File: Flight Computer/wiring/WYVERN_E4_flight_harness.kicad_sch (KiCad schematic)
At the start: 0 parts

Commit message: Commit!
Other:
- note added: "BATTERY SENSE (GP26 / ADC0)"
- note added: "GP26: ADC0 battery divider (100k/62k)"
- note added: "GP26: ADC0 node, ratio 0.3827 (8.4V -> 3.21V)"
- note added: "GP28: ADC2 spare (unwired)"
- note added: "R_BOT: 62k -> GND"
- note added: "R_TOP: 100k -> ADC node"
- note added: "VBAT_TAP: pack + (before UBEC)"
- note added: "warn 6.4V (3.2V/cell) / arm-inhibit 6.0V (3.0V/cell)"
- title: WYVERN-E 4.0 — RPi Pico 2 W flight harness -> WYVERN-E — RPi Pico 2 W flight harness

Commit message: Update - but the PCB no work :(
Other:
- note added: "+V (buck rail)"
- note added: "3V3(?)/GND: full-rate flight log"
- note added: "3V3: logic + sensor rail"
- note added: "A1 addr pin: traces to ~5V (R10/U13 node), not a valid GND/VS+/SDA/SCL strap"
- note added: "AP2112K-3.3 LDO -> 3V3 logic"
- note added: "BME680 (0x76 CONFIRMED, shared bus)"
- note added: "GP0/GP1: shared I2C -> body BNO055, external BNO085 (STEMMA-QT), BME680, INA226, LIS3MDL"
- note added: "GP12: reserved for RBF, NOT wired to any switch on this board rev"
- note added: "GP2: PWM servo1 (pitch, JST U8)"
- note added: "GP34: buzzer (H1 pin10, confirmed GPIO)"
- note added: "GP35: status LED (H1 pin9, confirmed GPIO)"
- note added: "GP36: CAM_EN gate (H1 pin8, confirmed GPIO)"
- note added: "GP37: LAUNCH_IRQ (H1 pin7, confirmed GPIO)"
- note added: "GP3: PWM servo2 (yaw, JST U9)"
- note added: "GP4/GP5: spare JST (U10/U11, function TBD)"
- note added: "GP8/GP9/GP10/GP11: microSD (MISO/CS/SCK/MOSI, all 4 pins confirmed)"
- note added: "IMUs x2, shared bus (different chip families)"
- note added: "INA226 POWER MONITOR (U4, shared I2C bus) -- WIRING PROBLEM, SEE CONFLICTS.md"
- note added: "LIS3MDL (0x1C CONFIRMED, shared bus)"
- note added: "MISO GP8 / CS GP9 / SCK GP10 / MOSI GP11 -- all confirmed (fixed a MOSI/CS swap from an earlier pass)"
- note added: "RP2350B (U1, bare QFN-80, custom PCB1)"
- note added: "S1_SIG: GP2 (JST U8)"
- note added: "S2_SIG: GP3 (JST U9)"
- note added: "SDO->GND, CSB->3V3 (I2C mode) -- pressure/temp/gas, no BMP388 populated"
- note added: "SDO/SA1->GND -- magnetometer, present on PCB1, unused by firmware"
- note added: "STORAGE, microSD (CARD1, TF-01A) -- POSSIBLE DEFECT, SEE CONFLICTS.md"
- note added: "TPS564201 buck -> intermediate rail"
- note added: "V(buck): gated by CAM_EN (GP36)"
- note added: "VBUS/VIN-: trace to the ~5V BUCK OUTPUT rail, not pack voltage"
- note added: "VIN+: traces to GND -- no real shunt in this path, current/power not meaningful"
- note added: "address 0x40 is a bench-scan starting guess, not confirmed"
- note added: "body: BNO055 0x28 CONFIRMED (COM3/ADR -> GND)"
- note added: "external: BNO085 0x4A (SH2 protocol, STEMMA-QT, bulkhead-boundary mount, not on the gimbal)"
- note added: "getBusVoltage() -> battery.h, rail-sag thresholds only (NOT LiPo pack protection)"
- note added: "no WiFi/BLE chip on this board -- wifi_telemetry.h compiled only if WIFI_ENABLED"
- note added: "pin4 (expected VDD) traces to GND in the netlist, not 3V3 -- bench-check before trusting SD logging"
- note added: "servo/expansion connectors (U8-U11) off buck rail"
- note removed: "+5V (UBEC rail)"
- note removed: "3V3 / GND: full-rate flight log"
- note removed: "3V3: sensor rail"
- note removed: "BATTERY SENSE (GP26 / ADC0)"
- note removed: "CYW43: WiFi/BLE bench telemetry"
- note removed: "GP14: PWM servo1 (pitch)"
- note removed: "GP15: PWM servo2 (yaw)"
- note removed: "GP16/GP17: I2C0 -> PCA9548A mux"
- note removed: "GP18/GP19: I2C1 -> gimbal BNO085"
- note removed: "GP2/3/4/5: SPI0 microSD (SCK/MOSI/MISO/CS)"
- note removed: "GP22: RBF sense"
- note removed: "GP26: ADC0 battery divider (100k/62k)"
- note removed: "GP26: ADC0 node, ratio 0.3827 (8.4V -> 3.21V)"
- note removed: "GP28: ADC2 spare (unwired)"
- note removed: "GP6/GP1: spare (RRC3 removed — motor ejection)"
- note removed: "GP7: LAUNCH_IRQ"
- note removed: "GP8: CAM_EN gate"
- note removed: "GP9: LED GP10: buzzer"
- note removed: "IMUs x3 (BNO085, Game Rotation Vector)"
- note removed: "PCA9548A I2C MUX (0x70, on I2C0)"
- note removed: "RPi PICO 2 W (RP2350, FC + real-time TVC)"
- note removed: "R_BOT: 62k -> GND"
- note removed: "R_TOP: 100k -> ADC node"
- note removed: "S1_SIG: GP14"
- note removed: "S2_SIG: GP15"
- note removed: "SCK GP2 / MOSI GP3 / MISO GP4 / CS GP5"
- note removed: "STORAGE — microSD (SPI0 breakout)"
- note removed: "V5: 5V UBEC -> Pico VSYS/cam/servos"
- note removed: "V5: gated by CAM_EN (GP8)"
- note removed: "VBAT_TAP: pack + (before UBEC)"
- note removed: "VSYS: 5V in"
- note removed: "body(FC): 0x4A mux ch0"
- note removed: "ch0: body BNO085 0x4A"
- note removed: "ch1: recovery BNO085 0x4A (vote)"
- note removed: "ch2: BME688 0x76"
- note removed: "ch3: BMP388 0x77 (Adafruit 3966, 3V3)"
- note removed: "ch4: spare (unpopulated)"
- note removed: "decouple: 1000uF@servos, 100uF+SS34->VSYS"
- note removed: "gimbal: 0x4A I2C1 (dedicated)"
- note removed: "recovery: 0x4A mux ch1 (vote)"
- note removed: "warn 6.4V (3.2V/cell) / arm-inhibit 6.0V (3.0V/cell)"
- title: WYVERN-E — RPi Pico 2 W flight harness -> WYVERN-E, RPi Pico 2 W flight harness

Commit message: Update!
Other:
- company: Skylight Rocketry -> Skylight Industries
- title: WYVERN-E, RPi Pico 2 W flight harness -> GTR70E WYVERN, RPi Pico 2 W flight harness
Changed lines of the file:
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@@
-(kicad_sch (version 20230121) (generator "wyvern4_wiring") (paper "A2")
-  (title_block (title "WYVERN-E, RPi Pico 2 W flight harness") (company "Skylight Rocketry") (rev "4.0"))
+(kicad_sch (version 20230121) (generator "gtr70e_wyvern_wiring") (paper "A2")
+  (title_block (title "GTR70E WYVERN, RPi Pico 2 W flight harness") (company "Skylight Industries") (rev "4.0"))
   (rectangle (start 20 20) (end 82 46) (stroke (width 0.25)(type solid)) (fill (type none)))
  (text "POWER" (at 22 23 0)(effects (font (size 1.6 1.6))(justify left)))

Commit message: update
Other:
- title: GTR70E WYVERN, RPi Pico 2 W flight harness -> GTR70E WYVERN, custom PCB1 (RP2350B) flight harness
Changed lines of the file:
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@@
 (kicad_sch (version 20230121) (generator "gtr70e_wyvern_wiring") (paper "A2")
-  (title_block (title "GTR70E WYVERN, RPi Pico 2 W flight harness") (company "Skylight Industries") (rev "4.0"))
+  (title_block (title "GTR70E WYVERN, custom PCB1 (RP2350B) flight harness") (company "Skylight Industries") (rev "4.0"))
   (rectangle (start 20 20) (end 82 46) (stroke (width 0.25)(type solid)) (fill (type none)))
  (text "POWER" (at 22 23 0)(effects (font (size 1.6 1.6))(justify left)))

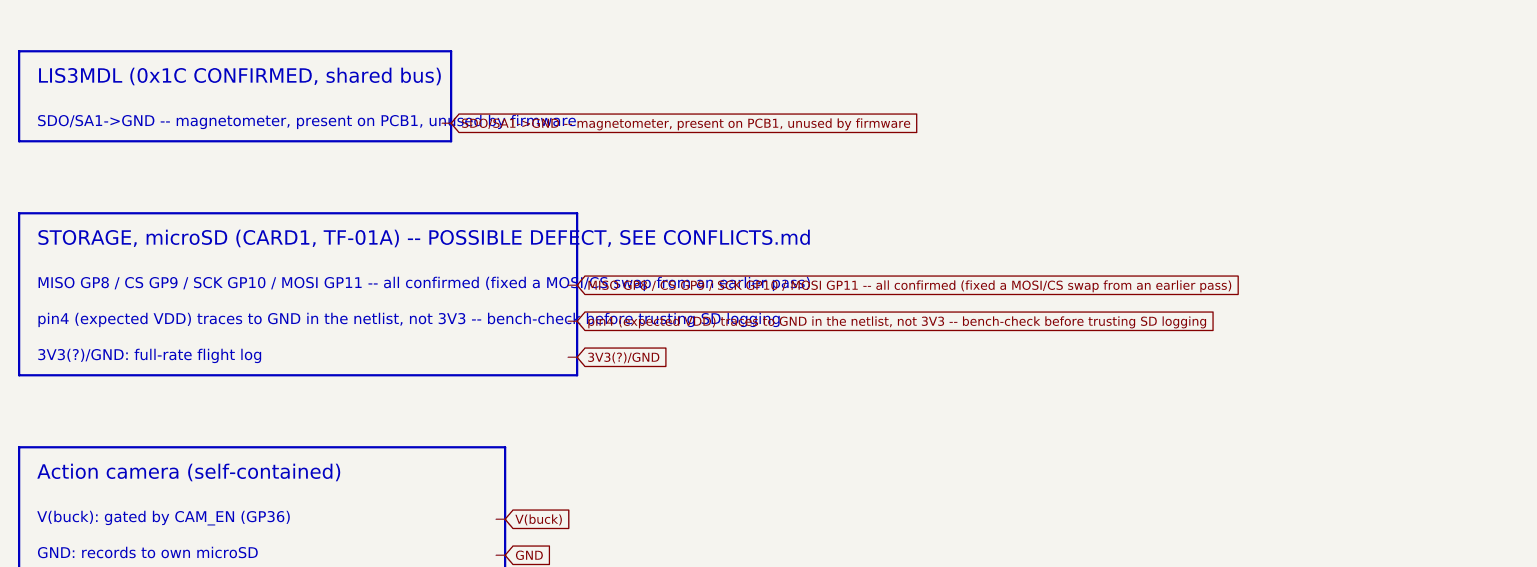
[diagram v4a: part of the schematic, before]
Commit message: Update ig... PCB still doesnt work :(
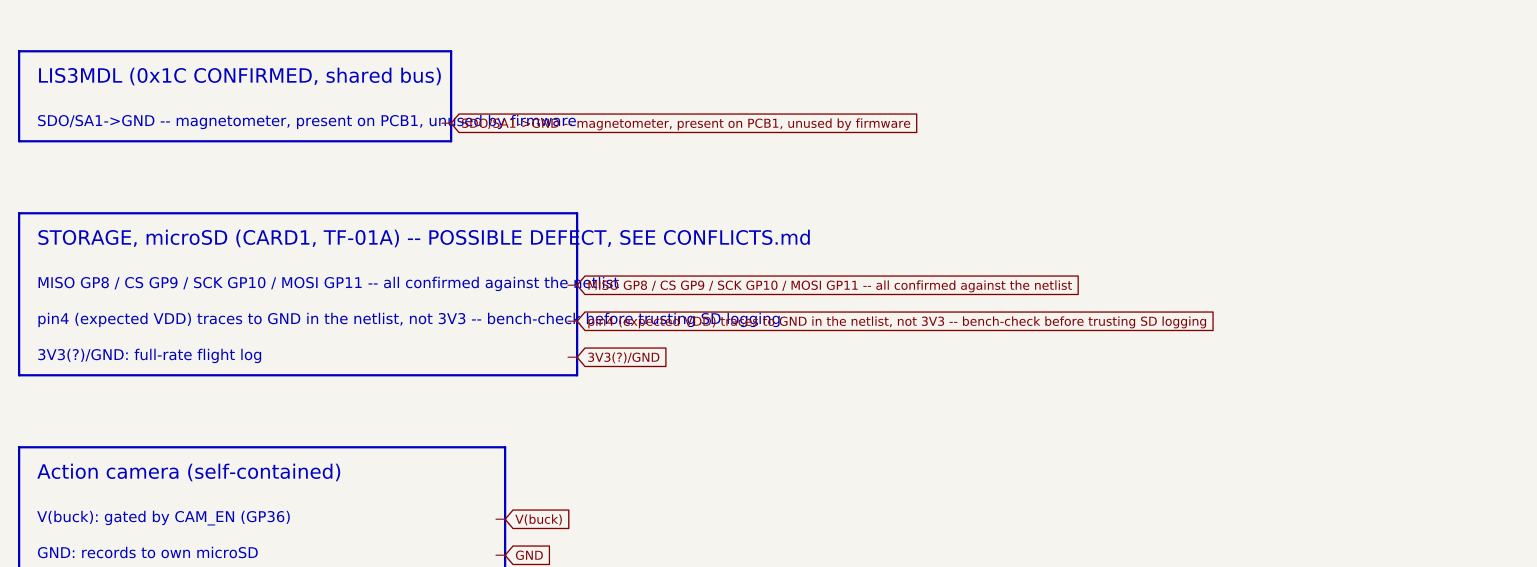
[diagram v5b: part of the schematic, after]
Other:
- note added: "MISO GP8 / CS GP9 / SCK GP10 / MOSI GP11 -- all confirmed against the netlist"
- note removed: "MISO GP8 / CS GP9 / SCK GP10 / MOSI GP11 -- all confirmed (fixed a MOSI/CS swap from an earlier pass)"
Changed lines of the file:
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@@
  (rectangle (start 20 212) (end 82 230) (stroke (width 0.25)(type solid)) (fill (type none)))
  (text "STORAGE, microSD (CARD1, TF-01A) -- POSSIBLE DEFECT, SEE CONFLICTS.md" (at 22 215 0)(effects (font (size 1.6 1.6))(justify left)))
- (text "MISO GP8 / CS GP9 / SCK GP10 / MOSI GP11 -- all confirmed (fixed a MOSI/CS swap from an earlier pass)" (at 22 220 0)(effects (font (size 1.2 1.2))(justify left)))
- (global_label "MISO GP8 / CS GP9 / SCK GP10 / MOSI GP11 -- all confirmed (fixed a MOSI/CS swap from an earlier pass)" (shape input)(at 82 220 0)(effects (font (size 1.0 1.0))(justify left)))
+ (text "MISO GP8 / CS GP9 / SCK GP10 / MOSI GP11 -- all confirmed against the netlist" (at 22 220 0)(effects (font (size 1.2 1.2))(justify left)))
+ (global_label "MISO GP8 / CS GP9 / SCK GP10 / MOSI GP11 -- all confirmed against the netlist" (shape input)(at 82 220 0)(effects (font (size 1.0 1.0))(justify left)))
  (wire (pts (xy 81 220) (xy 82 220)) (stroke (width 0.15)(type solid)))
  (text "pin4 (expected VDD) traces to GND in the netlist, not 3V3 -- bench-check before trusting SD logging" (at 22 224 0)(effects (font (size 1.2 1.2))(justify left)))
